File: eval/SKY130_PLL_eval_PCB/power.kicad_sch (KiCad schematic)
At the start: 12 parts, among them J7 Conn_02x13_Odd_Even, U1 ADM7154ARDZ-1.8-R7

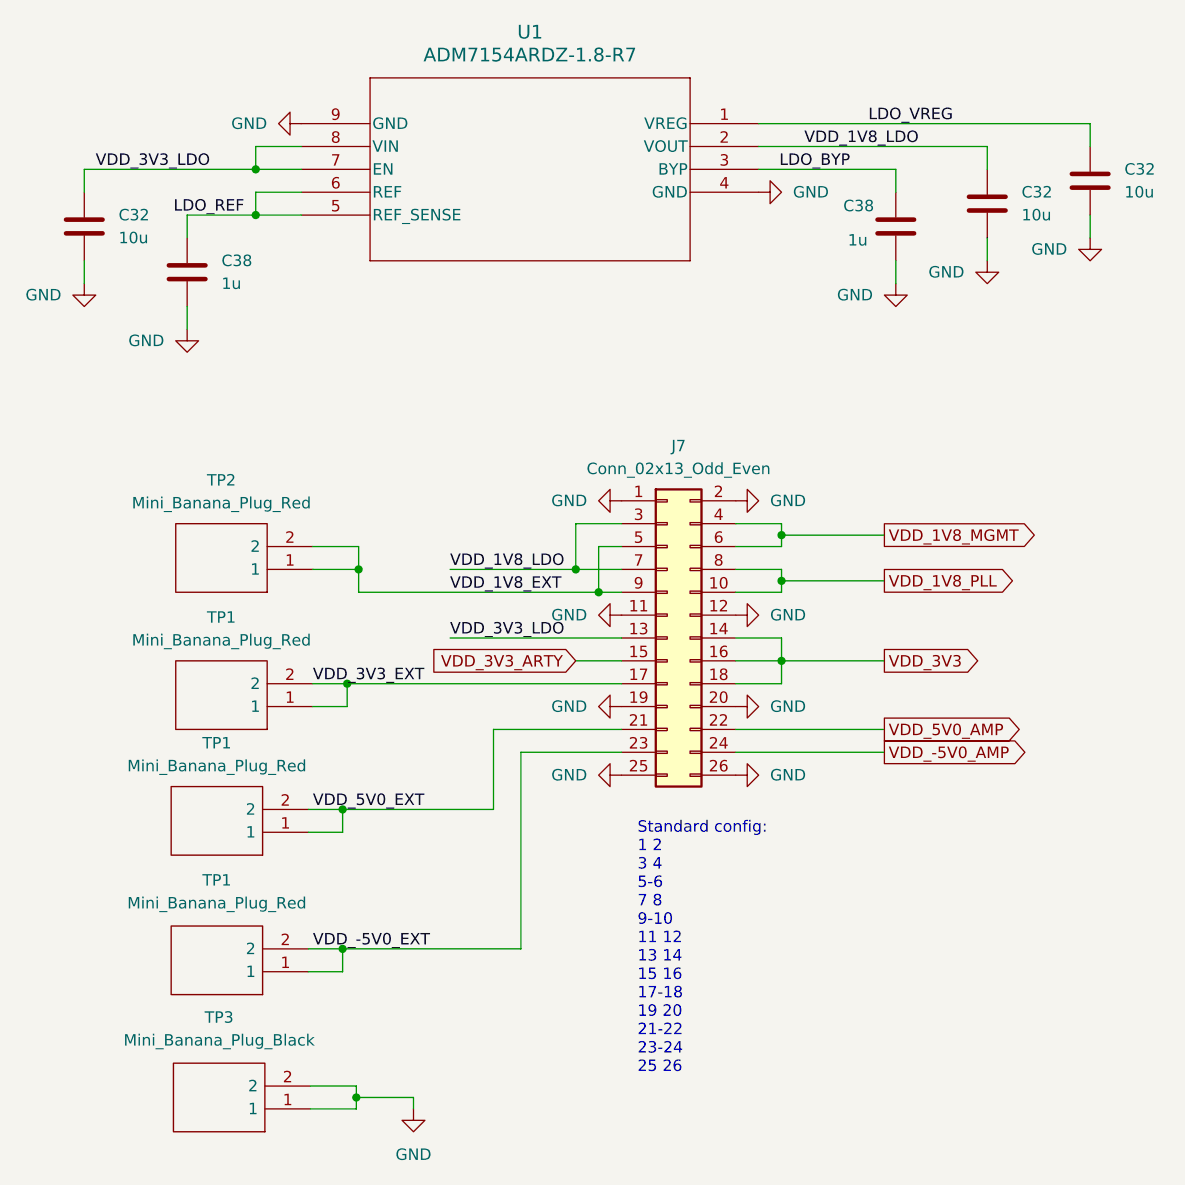
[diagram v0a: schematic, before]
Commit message: eval pcb added
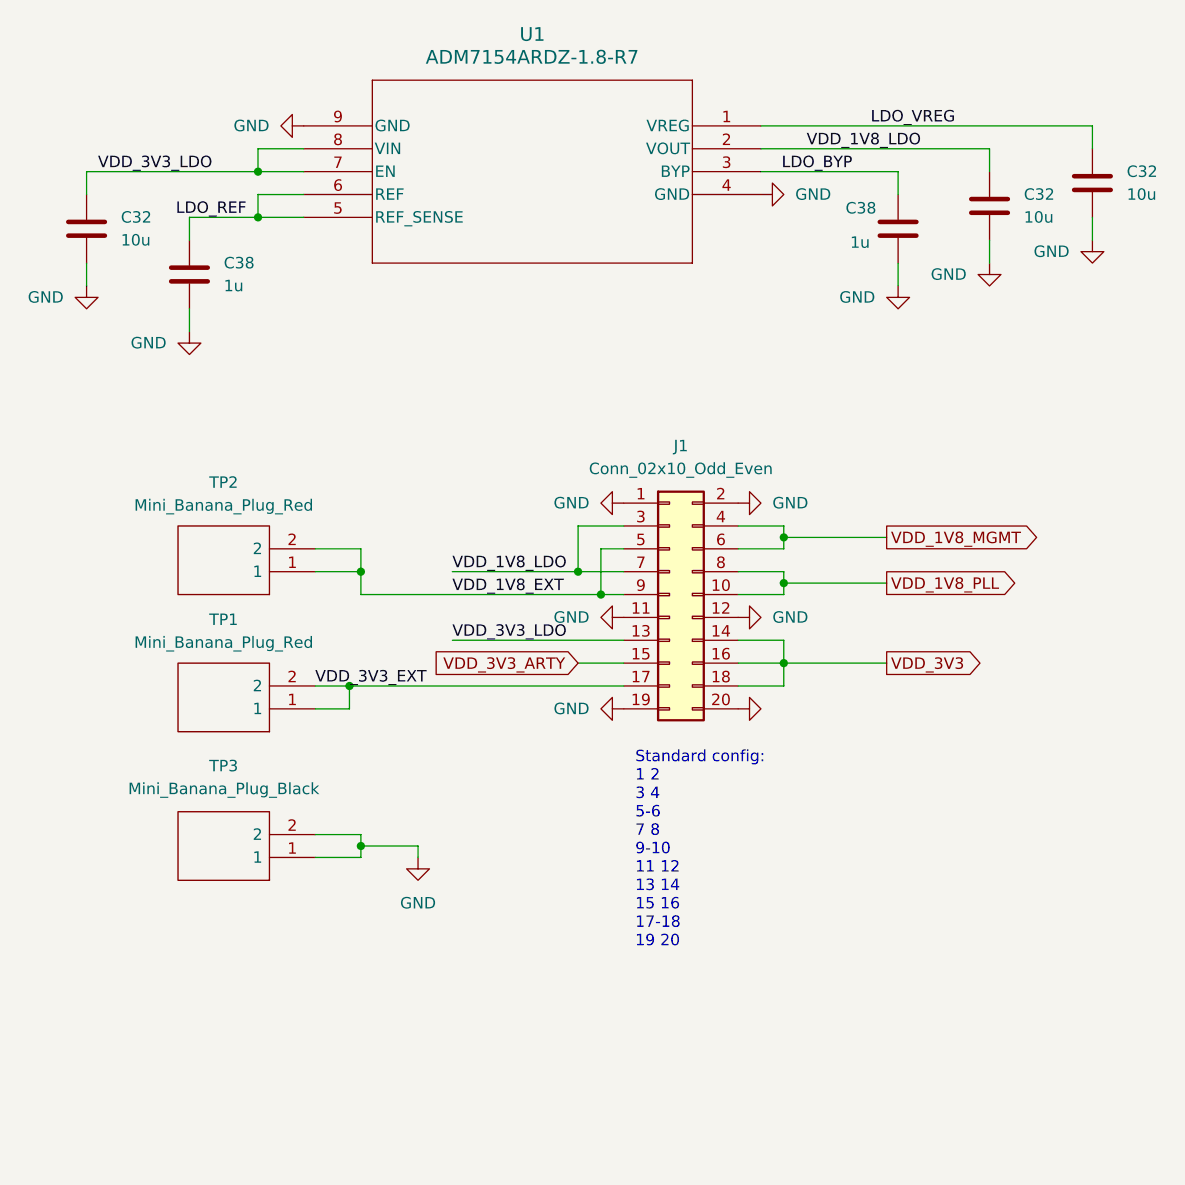
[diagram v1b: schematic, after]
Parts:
- removed J7: Conn_02x13_Odd_Even, Connector_PinHeader_2.54mm:PinHeader_2x13_P2.54mm_Vertical_SMD, symbol Connector_Generic:Conn_02x13_Odd_Even
- removed TP1 (x2): Mini_Banana_Plug_Red, TO_SENSO1:930224101, symbol TO_SENSO1:Mini_Banana_Plug_Red
- added J1: Conn_02x10_Odd_Even, Connector_PinHeader_2.54mm:PinHeader_2x10_P2.54mm_Vertical_SMD, symbol Connector_Generic:Conn_02x10_Odd_Even
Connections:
- net GND: now also J1.1 (Pin_1), J1.11 (Pin_11), J1.12 (Pin_12), J1.19 (Pin_19), J1.2 (Pin_2), J1.20 (Pin_20)
- net VDD_1V8_EXT: now also J1.5 (Pin_5), J1.9 (Pin_9)
- net VDD_1V8_LDO: now also J1.3 (Pin_3), J1.7 (Pin_7)
- net VDD_1V8_MGMT: now also J1.4 (Pin_4), J1.6 (Pin_6)
- net VDD_1V8_PLL: now also J1.10 (Pin_10), J1.8 (Pin_8)
- net VDD_3V3: now also J1.14 (Pin_14), J1.16 (Pin_16), J1.18 (Pin_18)
- net VDD_3V3_ARTY: now also J1.15 (Pin_15)
- net VDD_3V3_EXT: now also J1.17 (Pin_17)
- net VDD_3V3_LDO: now also J1.13 (Pin_13)
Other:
- note added: "Standard config: 1 2 3 4 5-6 7 8 9-10 11 12 13 14 15 16 17-18 19 20"
- note removed: "Standard config: 1 2 3 4 5-6 7 8 9-10 11 12 13 14 15 16 17-18 19 20 21-22 23-24 25 26"
- moved on the sheet: TP3

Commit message: version updated to Kicad 8.0
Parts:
- renumbered TP2 to TP1V8, TP1 to TP3V3, TP3 to TPGND1
